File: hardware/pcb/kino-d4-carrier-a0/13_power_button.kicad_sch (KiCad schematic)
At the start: 12 parts, among them J1300 POWER PUSHBUTTON, Q1300 2N7002, U1300 LTC2955ITS8-1

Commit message: feat(hardware): carrier A0.2 - power-side opens, power-button corner
- MB_3V3: three router links join the U900 group, R902 and the main rail.
- Gauge (U701): R701 (BIN pull-down) moves beside its pin, and R702 (GPOUT
  pull-up) moves to the board edge.
- PD controller (U1000): R1004 moves above pin 16, PD_VBUS_SENSE loops
  round it, and C1000 moves onto the USB_VBUS run.
- STAT and charge LED: the charger STAT pin has no layout path out of its
  power copper. It is left open, firmware reads the charge state over I2C,
  and the expander STAT input goes. D1301 (charge LED), R1304, R1109 and
  TP1100 leave the design.
- Power LED: R1303 and D1300 move below U1300.
- Power controller (U1300): C1301 moves beside pin 3. PB and EN drop
  through new vias, and EN runs along the bottom edge to Q1202.

DRC: no clearance or short errors, parity clean, ERC 0, 16 open
connections.

Co-Authored-By: Claude Opus 5.5 <noreply@anthropic.com>
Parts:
- removed D1301: LED AMBER, LED_SMD:LED_0603_1608Metric, symbol KINO_A0:D1301
- removed R1304: 2.2k, Resistor_SMD:R_0603_1608Metric, symbol KINO_A0:R1304
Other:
- note added: "Power controller TS8 pin map checked against manufacturer package drawing; EN is pin 7. KILL is pulled high until software requests shutdown. Long-hold target remains provisional. One green power LED (D1300, on MB_3V3, so lit only while the camera runs); there is no charge LED: the charger STAT pin has no layout path out, and charge state is shown by firmware from the charger status read over I2C."
- note removed: "Power controller TS8 pin map checked against manufacturer package drawing; EN is pin 7. KILL is pulled high until software requests shutdown. Long-hold target remains provisional."
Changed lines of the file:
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@@
       (company "KINO") (comment 1 "ENGINEERING DRAFT - NOT FOR FABRICATION"))
 (text "Hardware on/off and user indication" (at 15 12 0) (effects (font (size 2.5 2.5)) (justify left top)))
-(text "Power controller TS8 pin map checked against manufacturer package drawing; EN is pin 7. KILL is pulled high until software requests shutdown. Long-hold target remains provisional." (at 15 20 0) (effects (font (size 1.05 1.05)) (justify left top)))
+(text "Power controller TS8 pin map checked against manufacturer package drawing; EN is pin 7. KILL is pulled high until software requests shutdown. Long-hold target remains provisional. One green power LED (D1300, on MB_3V3, so lit only while the camera runs); there is no charge LED: the charger STAT pin has no layout path out, and charge state is shown by firmware from the charger status read over I2C." (at 15 20 0) (effects (font (size 1.05 1.05)) (justify left top)))
 (symbol (lib_id "KINO_A0:U1300") (at 73.66 55.879999999999995 0) (unit 1)
                   (in_bom yes) (on_board yes) (dnp no)
@@
                     (effects (font (size 0.9 0.9)) (justify left))
                     (property "Intersheetrefs" "${INTERSHEET_REFS}" (at 220.98000000000002 127.0 180) (effects (font (size 0.8 0.8)) (hide yes))))
-(symbol (lib_id "KINO_A0:R1304") (at 342.9 127.0 0) (unit 1)
-                  (in_bom yes) (on_board yes) (dnp no)
-                  (property "Reference" "R1304" (at 342.9 114.38 0) (effects (font (size 1.27 1.27))))
-                  (property "Value" "2.2k" (at 342.9 116.88 0) (effects (font (size 1.0 1.0))))
-                  (property "Footprint" "Resistor_SMD:R_0603_1608Metric" (at 342.9 127.0 0) (effects (font (size 1 1)) (hide yes)))
-                  (property "Datasheet" "https://www.yageogroup.com/component-documentation/download/specsheet/RC0603FR-072K2L" (at 342.9 127.0 0) (effects (font (size 1 1)) (hide yes)))
-                  (property "Design note" "" (at 342.9 127.0 0) (effects (font (size 1 1)) (hide yes)))
-                  (pin "1")(pin "2")
-                  (instances (project "KINO_D4_Carrier_A0" (path "/3e6ce248-02da-5043-9ed8-b7ca2a49de29/88235194-cd9f-573b-be45-1b4b1647b942" (reference "R1304") (unit 1)))))
-(wire (pts (xy 335.28 127.0) (xy 330.2 127.0)) (stroke (width 0) (type default)))
-(global_label "MB_3V3" (shape bidirectional) (at 330.2 127.0 0)
-                    (effects (font (size 0.9 0.9)) (justify right))
-                    (property "Intersheetrefs" "${INTERSHEET_REFS}" (at 330.2 127.0 0) (effects (font (size 0.8 0.8)) (hide yes))))
-(wire (pts (xy 350.52 127.0) (xy 355.59999999999997 127.0)) (stroke (width 0) (type default)))
-(global_label "CHARGE_LED_A" (shape bidirectional) (at 355.59999999999997 127.0 180)
-                    (effects (font (size 0.9 0.9)) (justify left))
-                    (property "Intersheetrefs" "${INTERSHEET_REFS}" (at 355.59999999999997 127.0 180) (effects (font (size 0.8 0.8)) (hide yes))))
-(symbol (lib_id "KINO_A0:D1301") (at 477.52 127.0 0) (unit 1)
-                  (in_bom yes) (on_board yes) (dnp no)
-                  (property "Reference" "D1301" (at 477.52 114.38 0) (effects (font (size 1.27 1.27))))
-                  (property "Value" "LED AMBER" (at 477.52 116.88 0) (effects (font (size 1.0 1.0))))
-                  (property "Footprint" "LED_SMD:LED_0603_1608Metric" (at 477.52 127.0 0) (effects (font (size 1 1)) (hide yes)))
-                  (property "Datasheet" "https://www.we-online.com/components/products/datasheet/150060AS75000.pdf" (at 477.52 127.0 0) (effects (font (size 1 1)) (hide yes)))
-                  (property "Design note" "" (at 477.52 127.0 0) (effects (font (size 1 1)) (hide yes)))
-                  (pin "1")(pin "2")
-                  (instances (project "KINO_D4_Carrier_A0" (path "/3e6ce248-02da-5043-9ed8-b7ca2a49de29/88235194-cd9f-573b-be45-1b4b1647b942" (reference "D1301") (unit 1)))))
-(wire (pts (xy 469.9 127.0) (xy 464.82 127.0)) (stroke (width 0) (type default)))
-(global_label "CHARGE_STAT_N" (shape bidirectional) (at 464.82 127.0 0)
-                    (effects (font (size 0.9 0.9)) (justify right))
-                    (property "Intersheetrefs" "${INTERSHEET_REFS}" (at 464.82 127.0 0) (effects (font (size 0.8 0.8)) (hide yes))))
-(wire (pts (xy 485.14 127.0) (xy 490.21999999999997 127.0)) (stroke (width 0) (type default)))
-(global_label "CHARGE_LED_A" (shape bidirectional) (at 490.21999999999997 127.0 180)
-                    (effects (font (size 0.9 0.9)) (justify left))
-                    (property "Intersheetrefs" "${INTERSHEET_REFS}" (at 490.21999999999997 127.0 180) (effects (font (size 0.8 0.8)) (hide yes))))
 (embedded_fonts no))

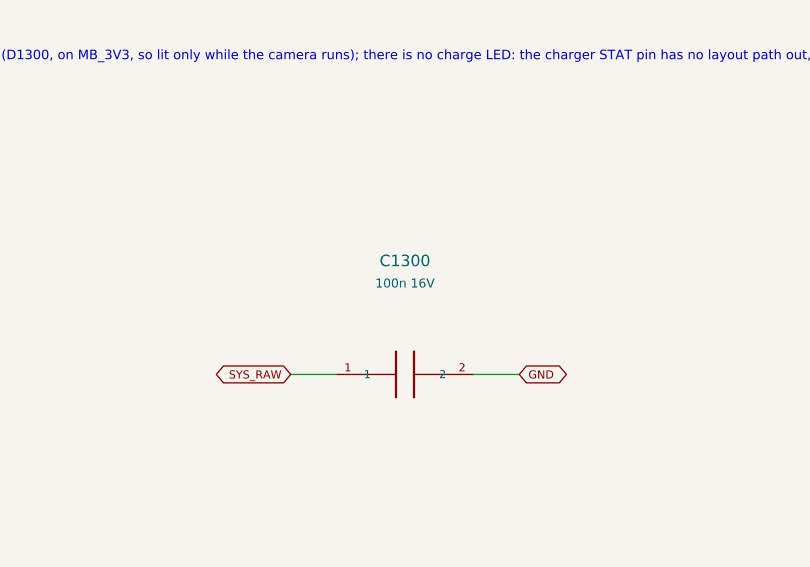
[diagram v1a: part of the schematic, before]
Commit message: feat(hardware): carrier A0.2 release pass - ready for fabrication with manual checks
Release review of the routed A0.2 carrier (A02-RELEASE.md: release matrix,
manual checks before ordering, bring-up tests). Final status: READY FOR
FABRICATION WITH SPECIFIC MANUAL CHECKS.

- USB-C input survives an unprogrammed STUSB4500 (20 V): D1001 SMF22A,
  R1004 10k, PD and load-switch P-FETs AO4409.
- Boost enable: R1204 100k BOOST_ENABLE to SYS_RAW (LTC2955-1 EN is a 2 uA
  source), Q1202 PMV16UN.
- I2C buffer U100 sides swapped (local bus on the TCA9517 A side's hard
  low); R100/R101 2.2k/22k hold EN low with JP1 pin 1 open.
- R105 SYNC_MASTER pull-down; D903 ESD on FN_N; TP1001 removed.
- SYS_RAW battery path as B.Cu and In2 pours with 25 extra vias; 1 oz inner
  copper in the stackup.
- XIAO socket pads get their solder-mask openings (footprint generator bug).
- Three fiducials per face; vias out of and away from pads; U1200 outline and
  pin-1 mark; legend lines and strokes 0.15 mm; silk association pass;
  CARRIER A0.2 / 2026-10 / S/N marking.
- Fab package (fab_a02.py): Gerbers + job file, drill, zip, placement files,
  fab BOM matched to LCSC by part number, hand-fit socket list, fab notes.
- Firmware constants header kino_carrier_a02.h.

DRC 0 / unconnected 0, ERC 0, verify.py --a02 passes.

Co-Authored-By: Claude Opus 5.5 <noreply@anthropic.com>
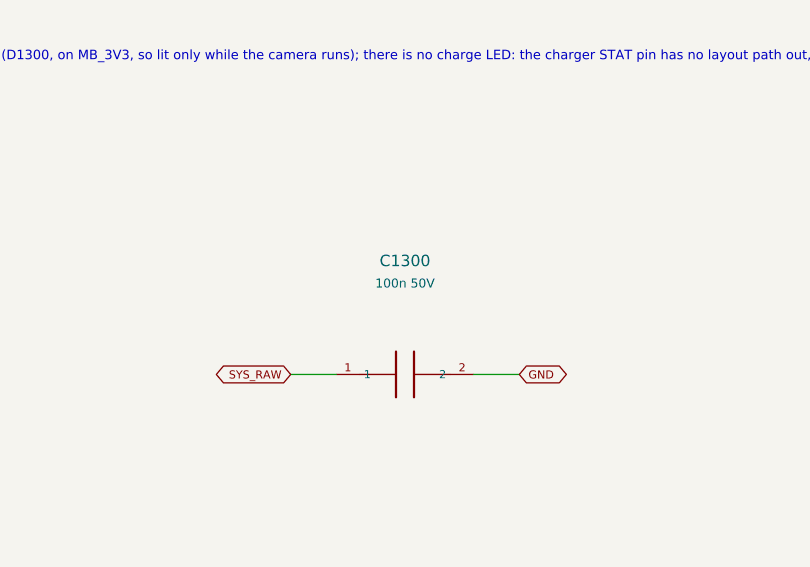
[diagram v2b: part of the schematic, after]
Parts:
- C1300: value 100n 16V -> 100n 50V
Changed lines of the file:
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@@
                   (in_bom yes) (on_board yes) (dnp no)
                   (property "Reference" "C1300" (at 208.28 43.26 0) (effects (font (size 1.27 1.27))))
-                  (property "Value" "100n 16V" (at 208.28 45.76 0) (effects (font (size 1.0 1.0))))
+                  (property "Value" "100n 50V" (at 208.28 45.76 0) (effects (font (size 1.0 1.0))))
                   (property "Footprint" "Capacitor_SMD:C_0603_1608Metric" (at 208.28 55.879999999999995 0) (effects (font (size 1 1)) (hide yes)))
                   (property "Datasheet" "https://www.yageogroup.com/component-documentation/download/specsheet/CC0603KRX7R9BB104" (at 208.28 55.879999999999995 0) (effects (font (size 1 1)) (hide yes)))
